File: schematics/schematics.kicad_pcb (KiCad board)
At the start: 4 copper layers, 96 x 35 mm, 35 parts, among them J1 2K, J2 SWD, J3 Micro SD Card, J4 POWER, SW1 RESET, U1 STM32F103VBT6, U2 AMS1117-3.3, Y1 16Mhz

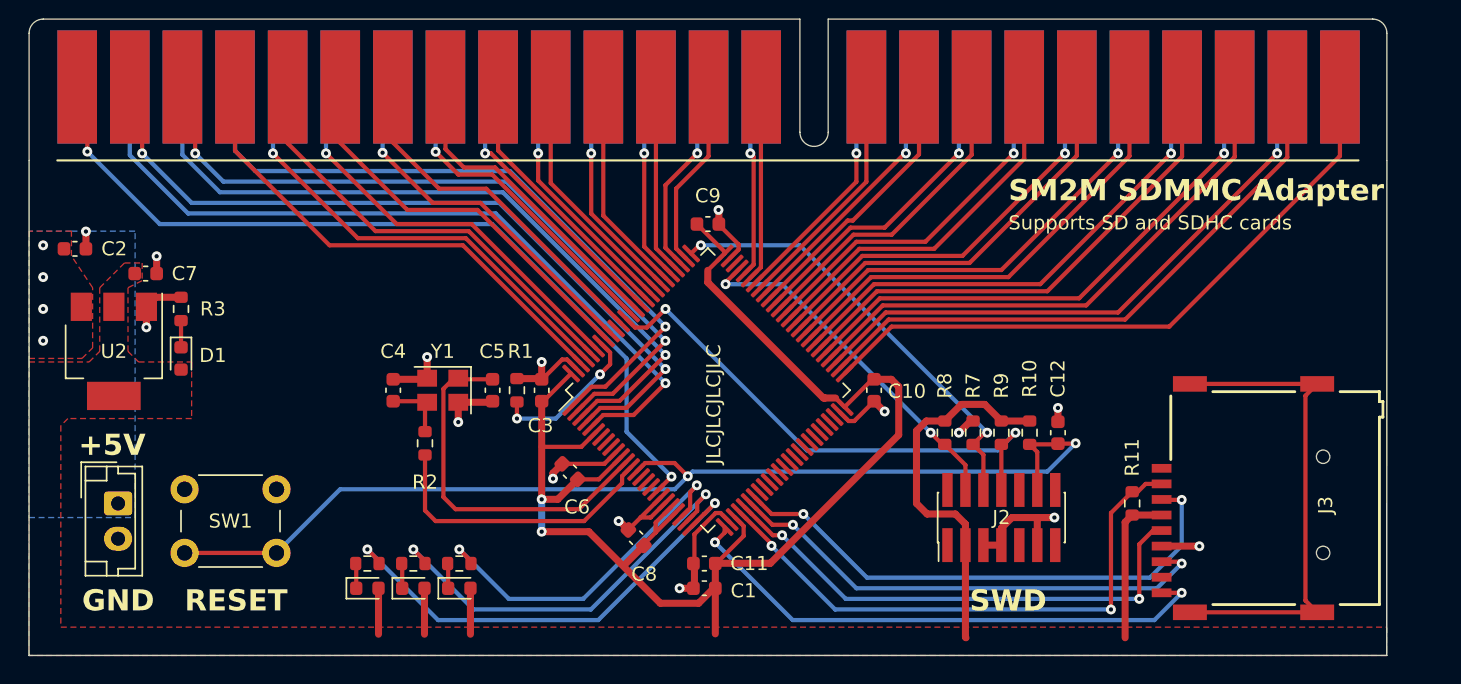
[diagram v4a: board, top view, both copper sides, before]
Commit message: Tune PCB trace spacing
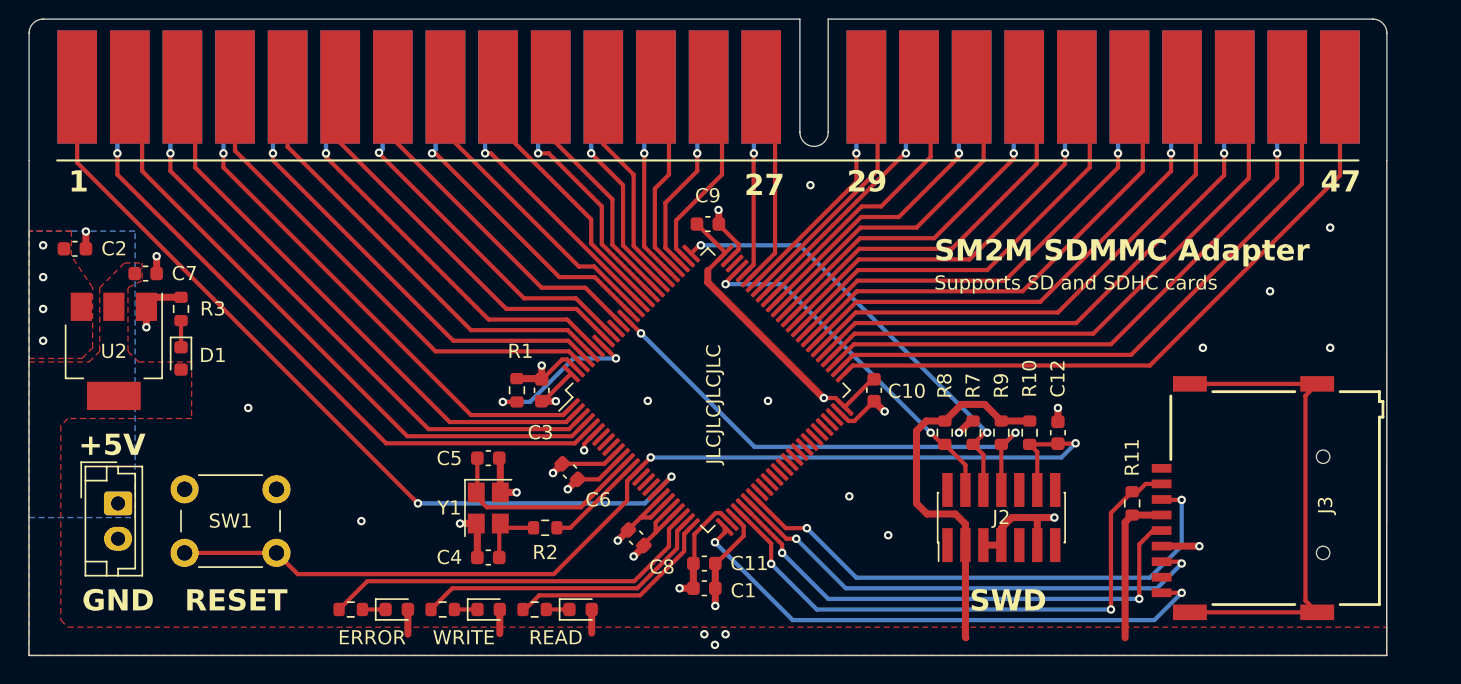
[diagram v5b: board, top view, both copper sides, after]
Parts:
- moved C4 13.6 mm to (133.5, 118.1), turned to 180 degrees
- moved R2 10.4 mm to (137.5, 116.0), turned to 0 degrees
- moved Y1 8.93 mm to (133.5, 114.6), turned to -90 degrees
- moved D2 8.71 mm to (140.0, 121.8)
- moved R4 6.24 mm to (136.8, 121.8), turned to 180 degrees
- moved D3 5.53 mm to (133.5, 121.8)
- moved C5 4.81 mm to (133.5, 111.0), turned to 0 degrees
- moved R5 3.86 mm to (130.2, 121.8), turned to 180 degrees
- moved R6 3.46 mm to (123.8, 121.8), turned to 180 degrees
- moved D4 2.56 mm to (127.0, 121.8)
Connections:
- net Data_Bus_Input_00 renamed DI_0
- net Data_Bus_Input_01 renamed DI_1
- net Data_Bus_Input_02 renamed DI_2
- net Data_Bus_Input_03 renamed DI_3
- net Data_Bus_Input_04 renamed DI_4
- net Data_Bus_Input_05 renamed DI_5
- net Data_Bus_Input_06 renamed DI_6
- net Data_Bus_Input_07 renamed DI_7
- net Data_Bus_Input_08 renamed DI_8
- net Data_Bus_Input_09 renamed DI_9
- net Data_Bus_Input_10 renamed DI_10
- net Data_Bus_Input_11 renamed DI_11
- net Data_Bus_Input_12 renamed DI_12
- net Data_Bus_Input_13 renamed DI_13
- net Data_Bus_Input_14 renamed DI_14
- net Data_Bus_Input_15 renamed DI_15
- net Data_Bus_Input_Control_0 renamed CTRLI_0
- net Data_Bus_Input_Control_1 renamed CTRLI_1
- net Data_Bus_Output_00 renamed DO_0
- net Data_Bus_Output_01 renamed DO_1
- net Data_Bus_Output_02 renamed DO_2
- net Data_Bus_Output_03 renamed DO_3
- net Data_Bus_Output_04 renamed DO_4
- net Data_Bus_Output_05 renamed DO_5
- net Data_Bus_Output_06 renamed DO_6
- net Data_Bus_Output_07 renamed DO_7
- net Data_Bus_Output_08 renamed DO_8
- net Data_Bus_Output_09 renamed DO_9
- net Data_Bus_Output_10 renamed DO_10
- net Data_Bus_Output_11 renamed DO_11
- net Data_Bus_Output_12 renamed DO_12
- net Data_Bus_Output_13 renamed DO_13
- net Data_Bus_Output_14 renamed DO_14
- net Data_Bus_Output_15 renamed DO_15
- net Data_Bus_Output_Control_0 renamed CTRLO_0
- net Data_Bus_Output_Control_1 renamed CTRLO_1
- net Data_Bus_Output_Control_State renamed CTRLD
- net Data_Transfer_Completed_Input renamed DTEI
- net Data_Transfer_Completed_Output renamed DTEO
- net Data_Transfer_Long_Input renamed DTLI
- net Data_Transfer_Short_Input renamed DTSI
- net External_Reset_Output renamed RSTE
- net External_Set_Output renamed SETE
- net Internal_Error_Output renamed ERR
- net Ready_Output renamed RDY
- net Reset_Input renamed RST
- net SDMMC_ERR_LED renamed SDMMC_WRITE_LED
- R4 pad 2: SDMMC_DETACHED_LED -> SDMMC_READ_LED
- R6 pad 2: BUS_ERR_LED -> SYSTEM_ERROR_LED
- U1 pad 23: SDMMC_DETACHED_LED -> SYSTEM_ERROR_LED
- U1 pad 25: BUS_ERR_LED -> SDMMC_READ_LED
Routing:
- net +3.3V: track 146.1 -> 88.5 mm, vias 2 -> 9
- net BUS_ERR_LED: track 33.8 -> 0.00 mm, vias 2 -> 0
- net SYSTEM_ERROR_LED: track 0.00 -> 27.6 mm
- net SDMMC_DETACHED_LED: track 25.6 -> 0.00 mm, vias 2 -> 0
- net SDMMC_READ_LED: track 0.00 -> 14.9 mm
- net OSC_OUT: track 20.7 -> 7.03 mm
- net DI_4: track 52.2 -> 40.8 mm, vias 2 -> 0
- net DI_3: track 49.1 -> 38.1 mm
- net OSC_IN: track 26.1 -> 15.2 mm
- net DI_5: track 55.5 -> 45.9 mm, vias 2 -> 0
- net DI_6: track 52.6 -> 43.2 mm
- net SDMMC_WRITE_LED: track 29.7 -> 21.3 mm, vias 2 -> 0
- net DI_7: track 55.7 -> 48.4 mm
- net DI_8: track 29.0 -> 25.2 mm
- net DTLI: track 42.8 -> 45.4 mm
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- added copper zone on In2.Cu, net +3.3V
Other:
- board text added: "1"
- board text added: "2"
- board text added: "27"
- board text added: "28"
- board text added: "29"
- board text added: "30"
- board text added: "47"
- board text added: "48"
- board text added: "ERROR"
- board text added: "Impedance control - JLC04161H-7628"
- board text added: "READ"
- board text added: "WRITE"
